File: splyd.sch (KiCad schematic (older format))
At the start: 260 parts

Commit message: Place all RGB LEDs
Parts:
- added R_LLED1, R_RLED1: 500, Resistor_SMD:R_0603_1608Metric, symbol Device:R
- renumbered CL00 to CL0, CL01 to CL1, CL02 to CL2, CL03 to CL3, CL04 to CL4, CL05 to CL5, CL06 to CL6, CR00 to CR0, CR01 to CR1, CR02 to CR2, CR03 to CR3, CR04 to CR4, CR05 to CR5, CR06 to CR6, DL00 to DL0, DL01 to DL1, DL02 to DL2, DL03 to DL3, DL04 to DL4, DL05 to DL5, DL06 to DL6, DR00 to DR0, DR01 to DR1, DR02 to DR2, DR03 to DR3, DR04 to DR4, DR05 to DR5, DR06 to DR6, KL00 to KL0, KL01 to KL1, KL02 to KL2, KL03 to KL3, KL04 to KL4, KL05 to KL5, KL06 to KL6, KR00 to KR0, KR01 to KR1, KR02 to KR2, KR03 to KR3, KR04 to KR4, KR05 to KR5, KR06 to KR6
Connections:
- net LLED: now also R_LLED1.1; no longer UL0.1 (TX0/PD3)
- net RLED: now also R_RLED1.2; no longer UR0.1 (TX0/PD3)
- new net: R_LLED1.2, UL0.1 (TX0/PD3)
- new net: R_RLED1.1, UR0.1 (TX0/PD3)

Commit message: Wire all LEDs on left thumb cluster
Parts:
- renumbered CL0 to CL00, CL1 to CL01, CL2 to CL02, CL3 to CL03, CL4 to CL04, CL5 to CL05, CL6 to CL06, CR0 to CR00, CR1 to CR01, CR2 to CR02, CR3 to CR03, CR4 to CR04, CR5 to CR05, CR6 to CR06, DL0 to DL00, DL1 to DL01, DL2 to DL02, DL3 to DL03, DL4 to DL04, DL5 to DL05, DL6 to DL06, DR0 to DR00, DR1 to DR01, DR2 to DR02, DR3 to DR03, DR4 to DR04, DR5 to DR05, DR6 to DR06, KL0 to KL00, KL1 to KL01, KL2 to KL02, KL3 to KL03, KL4 to KL04, KL5 to KL05, KL6 to KL06, KR0 to KR00, KR1 to KR01, KR2 to KR02, KR3 to KR03, KR4 to KR04, KR5 to KR05, KR6 to KR06

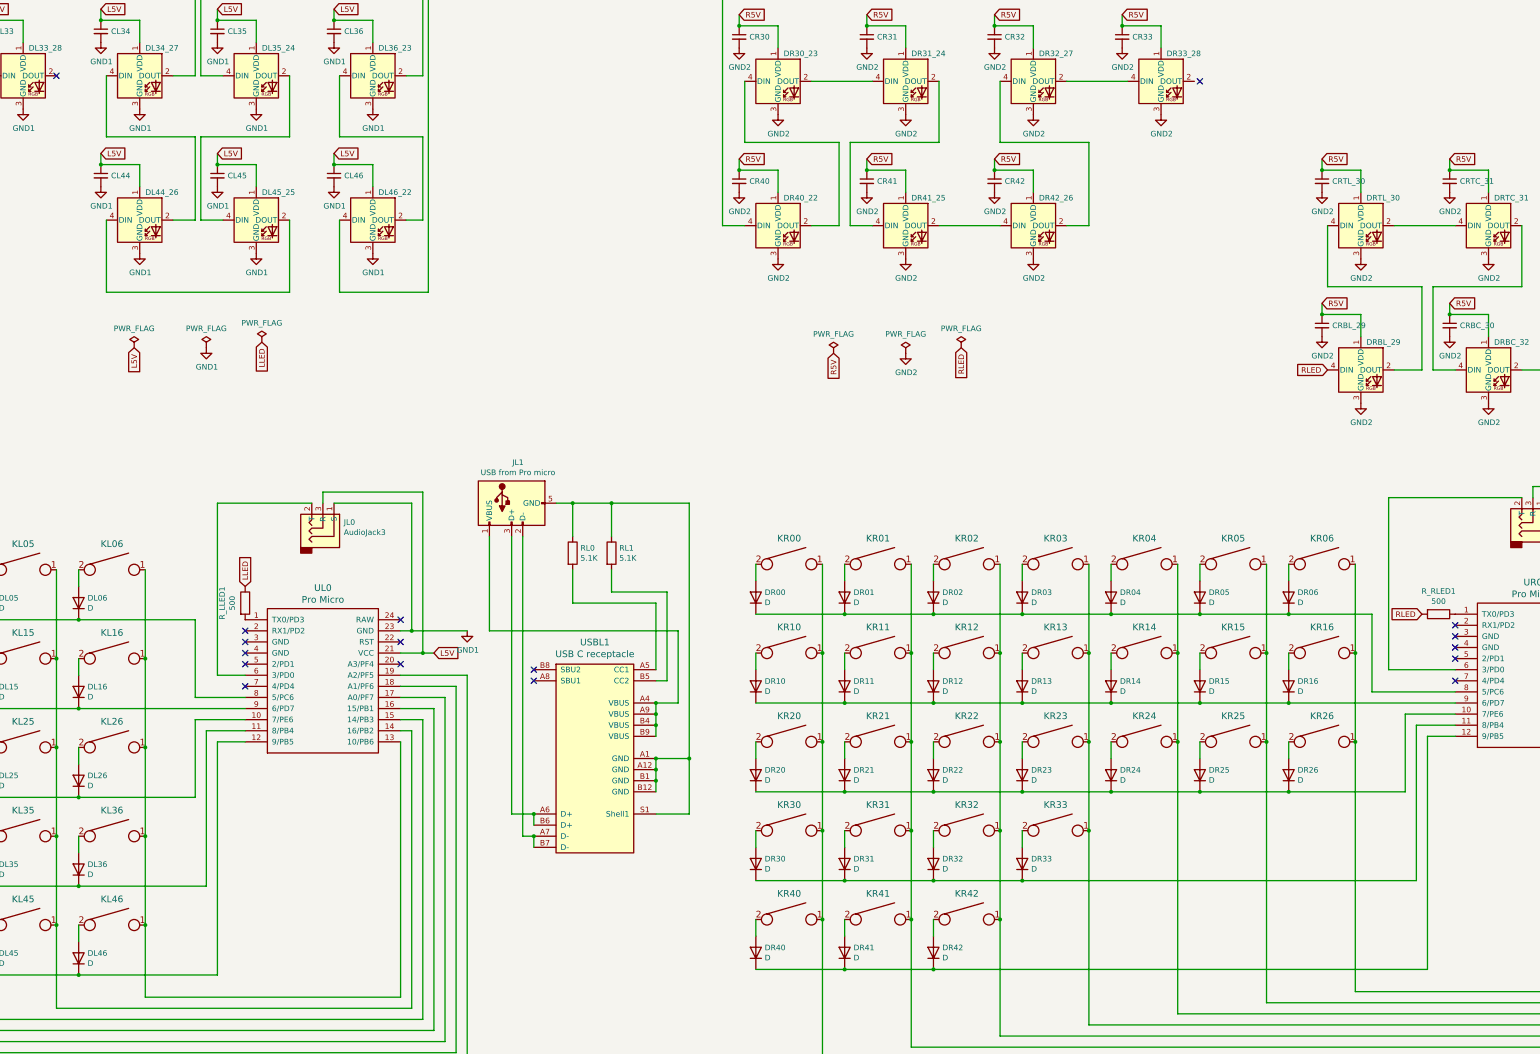
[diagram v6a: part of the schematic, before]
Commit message: Wire LED data to more suitable pin (shifts all row pins by 1)
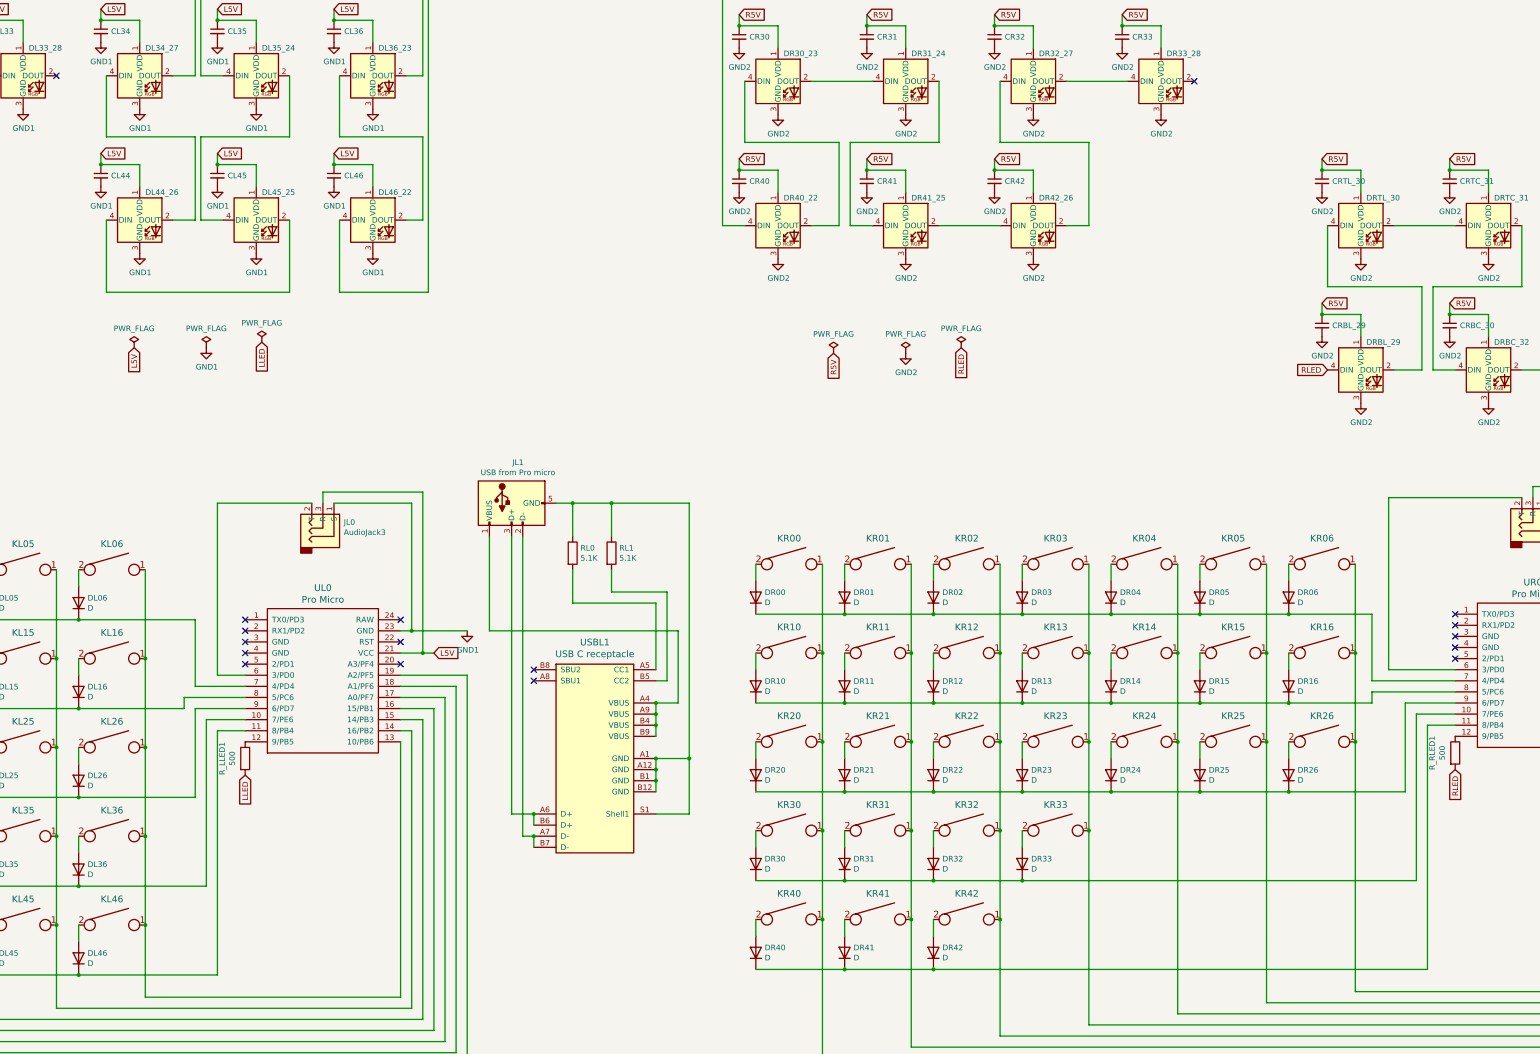
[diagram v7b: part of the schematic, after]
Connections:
- net LLED: now also R_LLED1.2; no longer R_LLED1.1
- net at DL00.1 (K), DL01.1 (K), DL02.1 (K)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: now also UL0.7 (4/PD4); no longer UL0.8 (5/PC6)
- net at DL10.1 (K), DL11.1 (K), DL12.1 (K)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: now also UL0.8 (5/PC6); no longer UL0.9 (6/PD7)
- net at DL20.1 (K), DL21.1 (K), DL22.1 (K)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: now also UL0.9 (6/PD7); no longer UL0.10 (7/PE6)
- net at DL33.1 (K), DL34.1 (K), DL35.1 (K)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: now also UL0.10 (7/PE6); no longer UL0.11 (8/PB4)
- net at DL44.1 (K), DL45.1 (K), DL46.1 (K): now also UL0.11 (8/PB4); no longer UL0.12 (9/PB5)
- net at UL0.1 (TX0/PD3): no longer R_LLED1.2
- net at UR0.1 (TX0/PD3): no longer R_RLED1.1
- net at DR20.1 (K), DR21.1 (K), DR22.1 (K)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: now also UR0.9 (6/PD7); no longer UR0.10 (7/PE6)
- net at DR30.1 (K), DR31.1 (K), DR32.1 (K)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: now also UR0.10 (7/PE6); no longer UR0.11 (8/PB4)
- net at DR40.1 (K), DR41.1 (K), DR42.1 (K): now also UR0.11 (8/PB4); no longer UR0.12 (9/PB5)
- net at UR0.7 (4/PD4): now also DR00.1 (K), DR01.1 (K), DR02.1 (K), DR03.1 (K), DR04.1 (K), DR05.1 (K), DR06.1 (K)
- net at DR10.1 (K), DR11.1 (K), DR12.1 (K)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: now also UR0.8 (5/PC6); no longer UR0.9 (6/PD7)
- new net: R_LLED1.1, UL0.12 (9/PB5)
- new net: R_RLED1.1, UR0.12 (9/PB5)
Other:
- moved on the sheet: R_LLED1, R_RLED1
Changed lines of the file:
@@
 	0    1    -1   0
 $EndComp
-NoConn ~ 9000 10850
 NoConn ~ 9000 10650
 NoConn ~ 9000 10450
@@
 	7600 10950 7350 10950
 Wire Wire Line
-	9600 10950 9000 10950
-Wire Wire Line
 	1900 14450 9600 14450
 Wire Wire Line
-	9500 11050 9000 11050
-Wire Wire Line
 	2700 14350 9500 14350
 Wire Wire Line
-	9400 11150 9000 11150
-Wire Wire Line
 	3500 14250 9400 14250
 Wire Wire Line
-	9300 11250 9000 11250
-Wire Wire Line
 	4300 14150 9300 14150
 Wire Wire Line
-	9200 11350 9000 11350
-Wire Wire Line
 	5100 14050 9200 14050
 Wire Wire Line
-	9100 11450 9000 11450
-Wire Wire Line
 	5900 13950 9100 13950
 Connection ~ 6700 13200
 Connection ~ 6100 13650
 Wire Wire Line
-	7350 11550 7600 11550
-Wire Wire Line
-	7350 13650 7350 11550
+	7350 11450 7600 11450
 Wire Wire Line
 	6100 13650 7350 13650
 Connection ~ 6100 12850
 Wire Wire Line
-	7250 11450 7600 11450
-Wire Wire Line
-	7250 12850 7250 11450
+	7250 11350 7600 11350
 Wire Wire Line
 	6100 12850 7250 12850
 Connection ~ 6100 12050
 Wire Wire Line
-	7150 11350 7600 11350
-Wire Wire Line
-	7150 12050 7150 11350
+	7150 11250 7600 11250
 Wire Wire Line
 	6100 12050 7150 12050
-Connection ~ 6100 11250
-Wire Wire Line
-	6100 11250 7600 11250
 Connection ~ 6100 10450
 Wire Wire Line
-	7150 11150 7600 11150
-Wire Wire Line
-	7150 10450 7150 11150
+	7150 11050 7600 11050
 Wire Wire Line
 	6100 10450 7150 10450
@@
 $EndComp
 Wire Wire Line
-	9600 10950 9600 14450
-Wire Wire Line
-	9500 11050 9500 14350
-Wire Wire Line
-	9400 11150 9400 14250
-Wire Wire Line
-	9300 11250 9300 14150
-Wire Wire Line
-	9200 11350 9200 14050
-Wire Wire Line
 	1900 11600 1900 14450
 Connection ~ 1900 11600
@@
 Connection ~ 5900 13200
 Wire Wire Line
-	9100 11450 9100 13950
-Wire Wire Line
 	6700 13200 6700 13850
 Wire Wire Line
 	6700 13850 9000 13850
-Wire Wire Line
-	9000 11550 9000 13850
 $Comp
 L Device:R RL0
@@
 	1    0    0    -1
 $EndComp
-NoConn ~ 7600 11050
-NoConn ~ 18500 11000
 $Comp
 L Device:R RR1
@@
 	17000 10400 17750 10400
 Wire Wire Line
-	17750 10400 17750 11100
+	17750 10400 17750 11000
 Connection ~ 17000 10400
 Wire Wire Line
-	17000 11200 18500 11200
-Connection ~ 17000 11200
-Wire Wire Line
 	17000 12000 18050 12000
 Wire Wire Line
-	18050 12000 18050 11300
-Wire Wire Line
-	18050 11300 18500 11300
+	18050 11200 18500 11200
 Connection ~ 17000 12000
 Wire Wire Line
-	18150 12800 18150 11400
-Wire Wire Line
-	18150 11400 18500 11400
+	18150 11300 18500 11300
 Wire Wire Line
-	18250 13600 18250 11500
-Wire Wire Line
-	18250 11500 18500 11500
+	18250 11400 18500 11400
 Wire Wire Line
 	20000 11400 19900 11400
@@
 Wire Wire Line
 	14400 9950 14400 10750
-Text GLabel 7600 10150 1    50   Input ~ 0
-LLED
-$Comp
-L keebio:ProMicro UL0
-U 1 1 5F5EA089
-P 8300 11000
-F 0 "UL0" H 8300 11837 60  0000 C CNN
-F 1 "Pro Micro" H 8300 11731 60  0000 C CNN
-F 2 "Keebio-Parts:ArduinoProMicro-ZigZag" V 9350 8500 60  0001 C CNN
-F 3 "" V 9350 8500 60  0001 C CNN
-	1    8300 11000
-	1    0    0    -1
-$EndComp
 Wire Wire Line
 	9200 10750 9300 10750
@@
 	20100 10700 20200 10700
 Connection ~ 20100 10700
-Text GLabel 18200 10400 0    50   Input ~ 0
+Text GLabel 18500 11800 3    50   Input ~ 0
 RLED
 Text GLabel 17350 8200 0    50   Input ~ 0
@@
 	1900 1650 2150 1650
 NoConn ~ 5900 5550
-NoConn ~ 16200 5600
+NoConn ~ 16150 5600
 Wire Wire Line
 	20250 6900 20450 6900
@@
 L Device:R R_RLED1
 U 1 1 62F9DC22
-P 18350 10400
-F 0 "R_RLED1" V 18143 10400 50  0000 C CNN
-F 1 "500" V 18234 10400 50  0000 C CNN
-F 2 "Resistor_SMD:R_0603_1608Metric" V 18280 10400 50  0001 C CNN
-F 3 "~" H 18350 10400 50  0001 C CNN
-	1    18350 10400
-	0    1    1    0
+P 18500 11650
+F 0 "R_RLED1" V 18293 11650 50  0000 C CNN
+F 1 "500" V 18384 11650 50  0000 C CNN
+F 2 "Resistor_SMD:R_0603_1608Metric" V 18430 11650 50  0001 C CNN
+F 3 "~" H 18500 11650 50  0001 C CNN
+	1    18500 11650
+	1    0    0    -1
 $EndComp
 Wire Wire Line
-	17750 11100 18500 11100
+	17750 11000 18500 11000
 Wire Wire Line
 	17900 10900 17900 9350
@@
 L Device:R R_LLED1
 U 1 1 63922A8A
-P 7600 10300
-F 0 "R_LLED1" V 7393 10300 50  0000 C CNN
-F 1 "500" V 7484 10300 50  0000 C CNN
-F 2 "Resistor_SMD:R_0603_1608Metric" V 7530 10300 50  0001 C CNN
-F 3 "~" H 7600 10300 50  0001 C CNN
-	1    7600 10300
+P 7600 11700
+F 0 "R_LLED1" V 7393 11700 50  0000 C CNN
+F 1 "500" V 7484 11700 50  0000 C CNN
+F 2 "Resistor_SMD:R_0603_1608Metric" V 7530 11700 50  0001 C CNN
+F 3 "~" H 7600 11700 50  0001 C CNN
+	1    7600 11700
 	1    0    0    -1
 $EndComp
+Text GLabel 7600 11850 3    50   Input ~ 0
+LLED
+Wire Wire Line
+	9000 11550 9000 13850
+NoConn ~ 9000 10850
+Wire Wire Line
+	9100 11450 9100 13950
+Wire Wire Line
+	9200 11350 9200 14050
+Wire Wire Line
+	9300 11250 9300 14150
+Wire Wire Line
+	9400 11150 9400 14250
+Wire Wire Line
+	9500 11050 9500 14350
+Wire Wire Line
+	9600 10950 9600 14450
+Wire Wire Line
+	9100 11450 9000 11450
+Wire Wire Line
+	9200 11350 9000 11350
+Wire Wire Line
+	9300 11250 9000 11250
+Wire Wire Line
+	9400 11150 9000 11150
+Wire Wire Line
+	9500 11050 9000 11050
+Wire Wire Line
+	9600 10950 9000 10950
+Wire Wire Line
+	7150 10450 7150 11050
+Wire Wire Line
+	7600 11150 7050 11150
+Wire Wire Line
+	7050 11150 7050 11250
+Wire Wire Line
+	7050 11250 6100 11250
+Connection ~ 6100 11250
+Wire Wire Line
+	7150 11250 7150 12050
+Wire Wire Line
+	7250 11350 7250 12850
+Wire Wire Line
+	7350 11450 7350 13650
+$Comp
+L keebio:ProMicro UL0
+U 1 1 5F5EA089
+P 8300 11000
+F 0 "UL0" H 8300 11837 60  0000 C CNN
+F 1 "Pro Micro" H 8300 11731 60  0000 C CNN
+F 2 "Keebio-Parts:ArduinoProMicro-ZigZag" V 9350 8500 60  0001 C CNN
+F 3 "" V 9350 8500 60  0001 C CNN
+	1    8300 11000
+	1    0    0    -1
+$EndComp
+NoConn ~ 7600 10450
+Wire Wire Line
+	18050 11200 18050 12000
+Wire Wire Line
+	18500 11100 17750 11100
+Wire Wire Line
+	17750 11100 17750 11200
+Wire Wire Line
+	17750 11200 17000 11200
+Connection ~ 17000 11200
+Wire Wire Line
+	18150 11300 18150 12800
+Wire Wire Line
+	18250 11400 18250 13600
+NoConn ~ 18500 10400
 $EndSCHEMATC

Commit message: Fill ground planes and panelize
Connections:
- net GND1: now also JL1.5 (GND), RL0.1, RL1.1, USBL1.A1 (GND), USBL1.A12 (GND), USBL1.B1 (GND), USBL1.B12 (GND), USBL1.S1 (Shell1)
- net GND2: now also JR1.5 (GND), RR0.1, RR1.1, USBR0.A1 (GND), USBR0.A12 (GND), USBR0.B1 (GND), USBR0.B12 (GND), USBR0.S1 (Shell1)
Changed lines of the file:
@@
 	18250 11400 18250 13600
 NoConn ~ 18500 10400
+Wire Wire Line
+	11600 9400 11850 9400
+Connection ~ 11600 9400
+$Comp
+L power:GND1 #PWR0241
+U 1 1 643BE796
+P 11850 9400
+F 0 "#PWR0241" H 11850 9150 50  0001 C CNN
+F 1 "GND1" H 11855 9227 50  0000 C CNN
+F 2 "" H 11850 9400 50  0001 C CNN
+F 3 "" H 11850 9400 50  0001 C CNN
+	1    11850 9400
+	1    0    0    -1
+$EndComp
+$Comp
+L power:GND2 #PWR0242
+U 1 1 643C109B
+P 22600 9350
+F 0 "#PWR0242" H 22600 9100 50  0001 C CNN
+F 1 "GND2" H 22605 9177 50  0000 C CNN
+F 2 "" H 22600 9350 50  0001 C CNN
+F 3 "" H 22600 9350 50  0001 C CNN
+	1    22600 9350
+	1    0    0    -1
+$EndComp
+Wire Wire Line
+	22500 9350 22600 9350
+Connection ~ 22500 9350
 $EndSCHEMATC
